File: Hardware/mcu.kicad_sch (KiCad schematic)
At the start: 10 parts, among them Q1 BSS138DW-7-F, U6 AS7341-DLGT

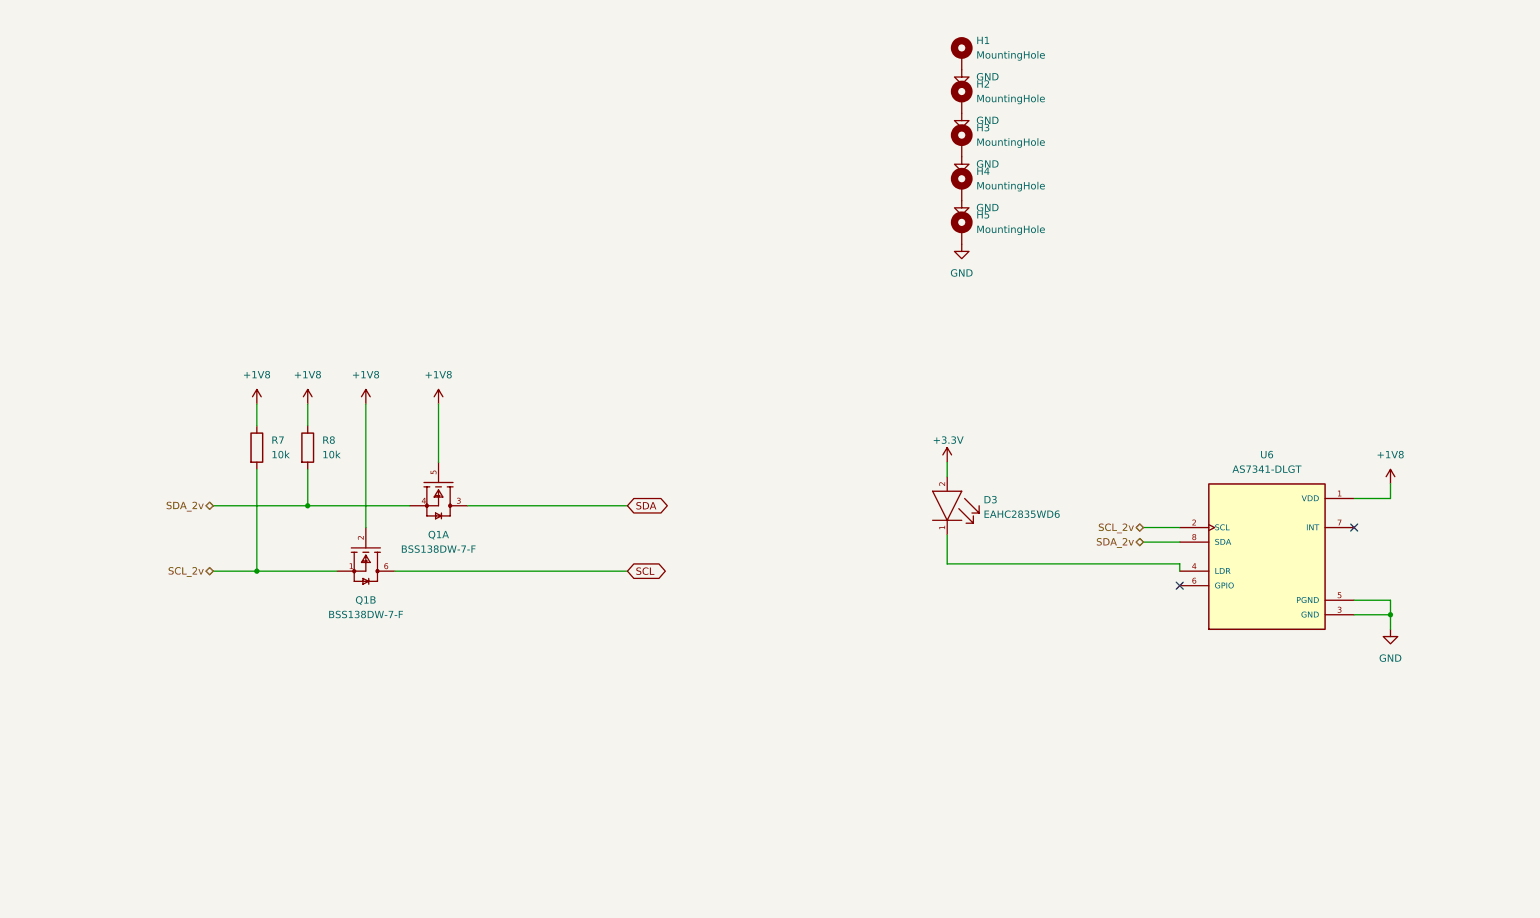
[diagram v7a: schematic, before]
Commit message: in the absence of design docs, I just did my own thing.  I've kept the ribbon cable, but I am not sure why there are one on either side, I've also brought out most of the interrupt lines on the through hole headers, the headers are designed for placement on a carrier board, negating the need for the ribbon cable when the board is stacked
Signed-off-by: lokimetasmith <lokimail@gmail.com>
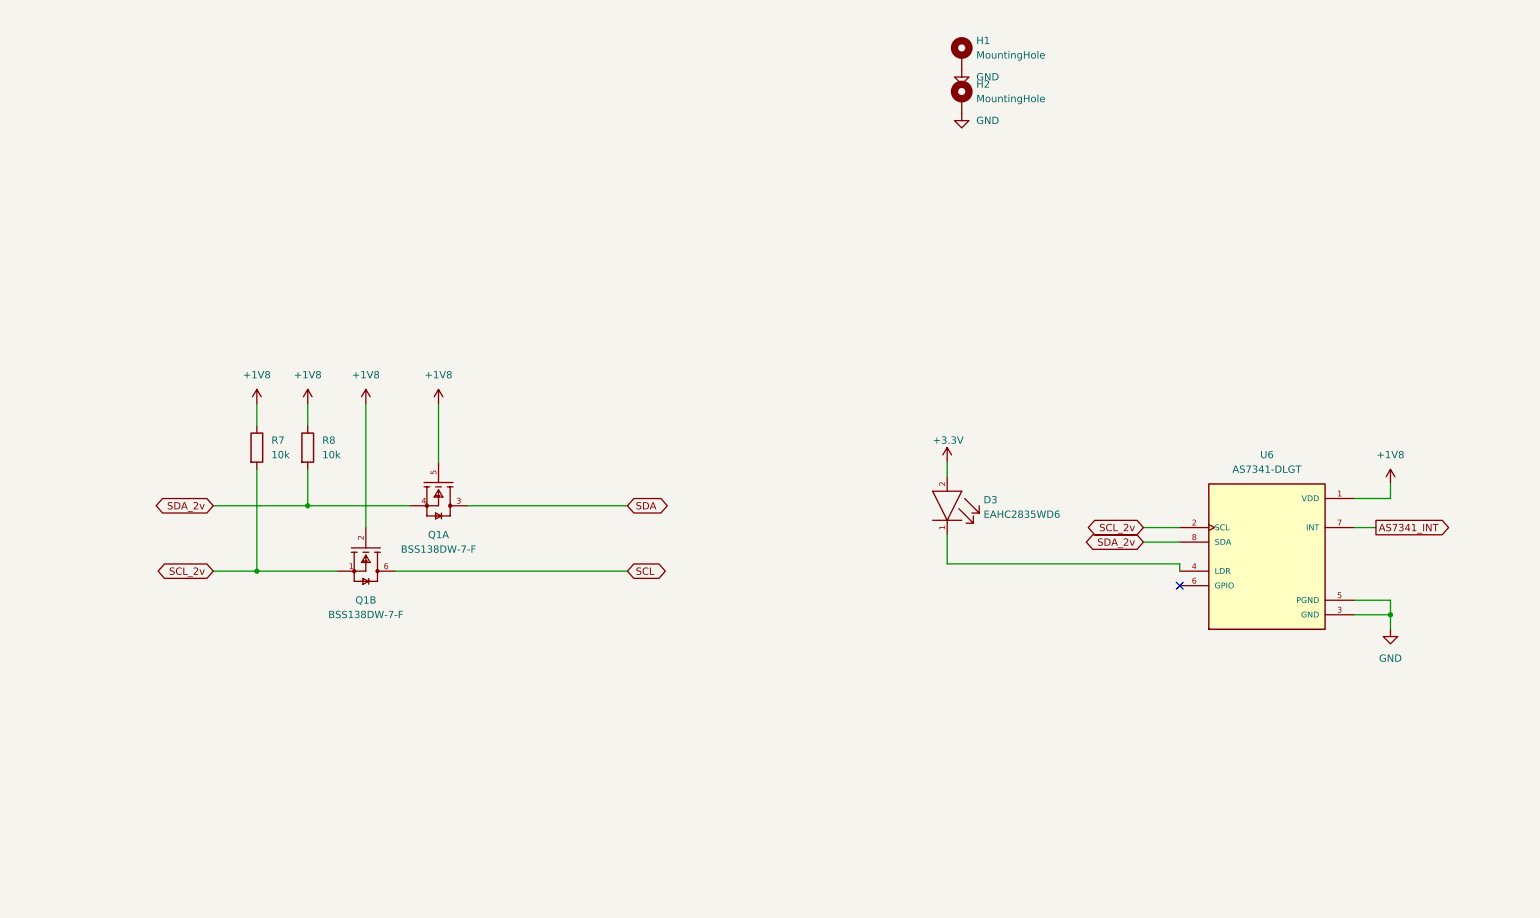
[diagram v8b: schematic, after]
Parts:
- removed H3, H4, H5: MountingHole, MountingHole:MountingHole_2.2mm_M2_ISO7380_Pad, symbol Mechanical:MountingHole_Pad
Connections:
- net AS7341_INT: now reaches U6.7 (INT)
- no-connect marks 2 -> 1
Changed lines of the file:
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@@
   (junction (at 68.58 110.49) (diameter 0) (color 0 0 0 0)
   )
-  (no_connect (at 251.46 114.3))
   (no_connect (at 220.98 124.46))
   (wire (pts (xy 180.34 102.87) (xy 180.34 105.41))
@@
     (stroke (width 0) (type default) (color 0 0 0 0))
   )
+  (wire (pts (xy 251.46 114.3) (xy 255.27 114.3))
+    (stroke (width 0) (type default) (color 0 0 0 0))
+  )
   (wire (pts (xy 68.58 104.14) (xy 68.58 110.49))
     (stroke (width 0) (type default) (color 0 0 0 0))
@@
   (wire (pts (xy 59.69 121.92) (xy 73.66 121.92))
     (stroke (width 0) (type default) (color 0 0 0 0))
+  )
+  (global_label "SCL_2v" (shape bidirectional) (at 52.07 121.92 180) (fields_autoplaced)
+    (effects (font (size 1.27 1.27)) (justify right))
+    (property "Intersheet References" "${INTERSHEET_REFS}" (id 0) (at 43.0045 121.8406 0)
+      (effects (font (size 1.27 1.27)) (justify right) hide)
+    )
+  )
+  (global_label "SDA_2v" (shape bidirectional) (at 214.63 116.84 180) (fields_autoplaced)
+    (effects (font (size 1.27 1.27)) (justify right))
+    (property "Intersheet References" "${INTERSHEET_REFS}" (id 0) (at 205.504 116.7606 0)
+      (effects (font (size 1.27 1.27)) (justify right) hide)
+    )
   )
   (global_label "SDA" (shape bidirectional) (at 124.46 110.49 0) (fields_autoplaced)
@@
     )
   )
+  (global_label "SDA_2v" (shape bidirectional) (at 52.07 110.49 180) (fields_autoplaced)
+    (effects (font (size 1.27 1.27)) (justify right))
+    (property "Intersheet References" "${INTERSHEET_REFS}" (id 0) (at 42.944 110.4106 0)
+      (effects (font (size 1.27 1.27)) (justify right) hide)
+    )
+  )
+  (global_label "SCL_2v" (shape bidirectional) (at 214.63 114.3 180) (fields_autoplaced)
+    (effects (font (size 1.27 1.27)) (justify right))
+    (property "Intersheet References" "${INTERSHEET_REFS}" (id 0) (at 205.5645 114.2206 0)
+      (effects (font (size 1.27 1.27)) (justify right) hide)
+    )
+  )
+  (global_label "AS7341_INT" (shape output) (at 255.27 114.3 0) (fields_autoplaced)
+    (effects (font (size 1.27 1.27)) (justify left))
+    (property "Intersheet References" "${INTERSHEET_REFS}" (id 0) (at 268.6898 114.2206 0)
+      (effects (font (size 1.27 1.27)) (justify left) hide)
+    )
+  )
   (global_label "SCL" (shape bidirectional) (at 124.46 121.92 0) (fields_autoplaced)
     (effects (font (size 1.27 1.27)) (justify left))
@@
     )
   )
-  (hierarchical_label "SCL_2v" (shape bidirectional) (at 52.07 121.92 180)
-    (effects (font (size 1.27 1.27)) (justify right))
-  )
-  (hierarchical_label "SDA_2v" (shape bidirectional) (at 52.07 110.49 180)
-    (effects (font (size 1.27 1.27)) (justify right))
-  )
-  (hierarchical_label "SDA_2v" (shape bidirectional) (at 214.63 116.84 180)
-    (effects (font (size 1.27 1.27)) (justify right))
-  )
-  (hierarchical_label "SCL_2v" (shape bidirectional) (at 214.63 114.3 180)
-    (effects (font (size 1.27 1.27)) (justify right))
-  )
   (symbol (lib_id "Device:R") (at 68.58 100.33 0) (unit 1)
     (in_bom yes) (on_board yes) (fields_autoplaced)
@@
     (pin "2")
   )
-  (symbol (lib_id "power:GND") (at 182.88 64.77 0) (unit 1)
-    (in_bom yes) (on_board yes) (fields_autoplaced)
-    (property "Reference" "#PWR0134" (id 0) (at 182.88 71.12 0)
-      (effects (font (size 1.27 1.27)) hide)
-    )
-    (property "Value" "GND" (id 1) (at 182.88 69.85 0))
-    (property "Footprint" "" (id 2) (at 182.88 64.77 0)
-      (effects (font (size 1.27 1.27)) hide)
-    )
-    (property "Datasheet" "" (id 3) (at 182.88 64.77 0)
-      (effects (font (size 1.27 1.27)) hide)
-    )
-    (pin "1")
-  )
   (symbol (lib_id "power:GND") (at 182.88 34.29 0) (unit 1)
     (in_bom yes) (on_board yes) (fields_autoplaced)
@@
     (pin "1")
     (pin "2")
-  )
-  (symbol (lib_id "Mechanical:MountingHole_Pad") (at 182.88 62.23 0) (unit 1)
-    (in_bom yes) (on_board yes) (fields_autoplaced)
-    (property "Reference" "H5" (id 0) (at 185.42 59.6899 0)
-      (effects (font (size 1.27 1.27)) (justify left))
-    )
-    (property "Value" "MountingHole" (id 1) (at 185.42 62.2299 0)
-      (effects (font (size 1.27 1.27)) (justify left))
-    )
-    (property "Footprint" "MountingHole:MountingHole_2.2mm_M2_ISO7380_Pad" (id 2) (at 182.88 62.23 0)
-      (effects (font (size 1.27 1.27)) hide)
-    )
-    (property "Datasheet" "~" (id 3) (at 182.88 62.23 0)
-      (effects (font (size 1.27 1.27)) hide)
-    )
-    (pin "1")
   )
   (symbol (lib_id "power:+3.3V") (at 180.34 102.87 0) (unit 1)
@@
     (pin "1")
   )
-  (symbol (lib_id "power:GND") (at 182.88 49.53 0) (unit 1)
-    (in_bom yes) (on_board yes) (fields_autoplaced)
-    (property "Reference" "#PWR0135" (id 0) (at 182.88 55.88 0)
-      (effects (font (size 1.27 1.27)) hide)
-    )
-    (property "Value" "GND" (id 1) (at 185.42 50.7999 0)
-      (effects (font (size 1.27 1.27)) (justify left))
-    )
-    (property "Footprint" "" (id 2) (at 182.88 49.53 0)
-      (effects (font (size 1.27 1.27)) hide)
-    )
-    (property "Datasheet" "" (id 3) (at 182.88 49.53 0)
-      (effects (font (size 1.27 1.27)) hide)
-    )
-    (pin "1")
-  )
-  (symbol (lib_id "Mechanical:MountingHole_Pad") (at 182.88 46.99 0) (unit 1)
-    (in_bom yes) (on_board yes) (fields_autoplaced)
-    (property "Reference" "H3" (id 0) (at 185.42 44.4499 0)
-      (effects (font (size 1.27 1.27)) (justify left))
-    )
-    (property "Value" "MountingHole" (id 1) (at 185.42 46.9899 0)
-      (effects (font (size 1.27 1.27)) (justify left))
-    )
-    (property "Footprint" "MountingHole:MountingHole_2.2mm_M2_ISO7380_Pad" (id 2) (at 182.88 46.99 0)
-      (effects (font (size 1.27 1.27)) hide)
-    )
-    (property "Datasheet" "~" (id 3) (at 182.88 46.99 0)
-      (effects (font (size 1.27 1.27)) hide)
-    )
-    (pin "1")
-  )
   (symbol (lib_id "Diodes_Inc._-_BSS138DW-7-F:BSS138DW-7-F") (at 91.44 100.33 270) (unit 1)
     (in_bom yes) (on_board yes) (fields_autoplaced)
@@
     (pin "1")
     (pin "2")
-  )
-  (symbol (lib_id "Mechanical:MountingHole_Pad") (at 182.88 54.61 0) (unit 1)
-    (in_bom yes) (on_board yes) (fields_autoplaced)
-    (property "Reference" "H4" (id 0) (at 185.42 52.0699 0)
-      (effects (font (size 1.27 1.27)) (justify left))
-    )
-    (property "Value" "MountingHole" (id 1) (at 185.42 54.6099 0)
-      (effects (font (size 1.27 1.27)) (justify left))
-    )
-    (property "Footprint" "MountingHole:MountingHole_2.2mm_M2_ISO7380_Pad" (id 2) (at 182.88 54.61 0)
-      (effects (font (size 1.27 1.27)) hide)
-    )
-    (property "Datasheet" "~" (id 3) (at 182.88 54.61 0)
-      (effects (font (size 1.27 1.27)) hide)
-    )
-    (pin "1")
   )
   (symbol (lib_id "AS7341-DLGT:AS7341-DLGT") (at 236.22 119.38 0) (unit 1)
@@
     (pin "8")
   )
-  (symbol (lib_id "power:GND") (at 182.88 57.15 0) (unit 1)
-    (in_bom yes) (on_board yes) (fields_autoplaced)
-    (property "Reference" "#PWR0133" (id 0) (at 182.88 63.5 0)
-      (effects (font (size 1.27 1.27)) hide)
-    )
-    (property "Value" "GND" (id 1) (at 185.42 58.4199 0)
-      (effects (font (size 1.27 1.27)) (justify left))
-    )
-    (property "Footprint" "" (id 2) (at 182.88 57.15 0)
-      (effects (font (size 1.27 1.27)) hide)
-    )
-    (property "Datasheet" "" (id 3) (at 182.88 57.15 0)
-      (effects (font (size 1.27 1.27)) hide)
-    )
-    (pin "1")
-  )
   (symbol (lib_id "Mechanical:MountingHole_Pad") (at 182.88 31.75 0) (unit 1)
